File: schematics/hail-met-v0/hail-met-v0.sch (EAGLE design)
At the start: 102 parts, among them IC1 MCP73871, J1 AVR_SPI_PRG_6PTH, U1 ATMEGA328P, Y1 16MHZ

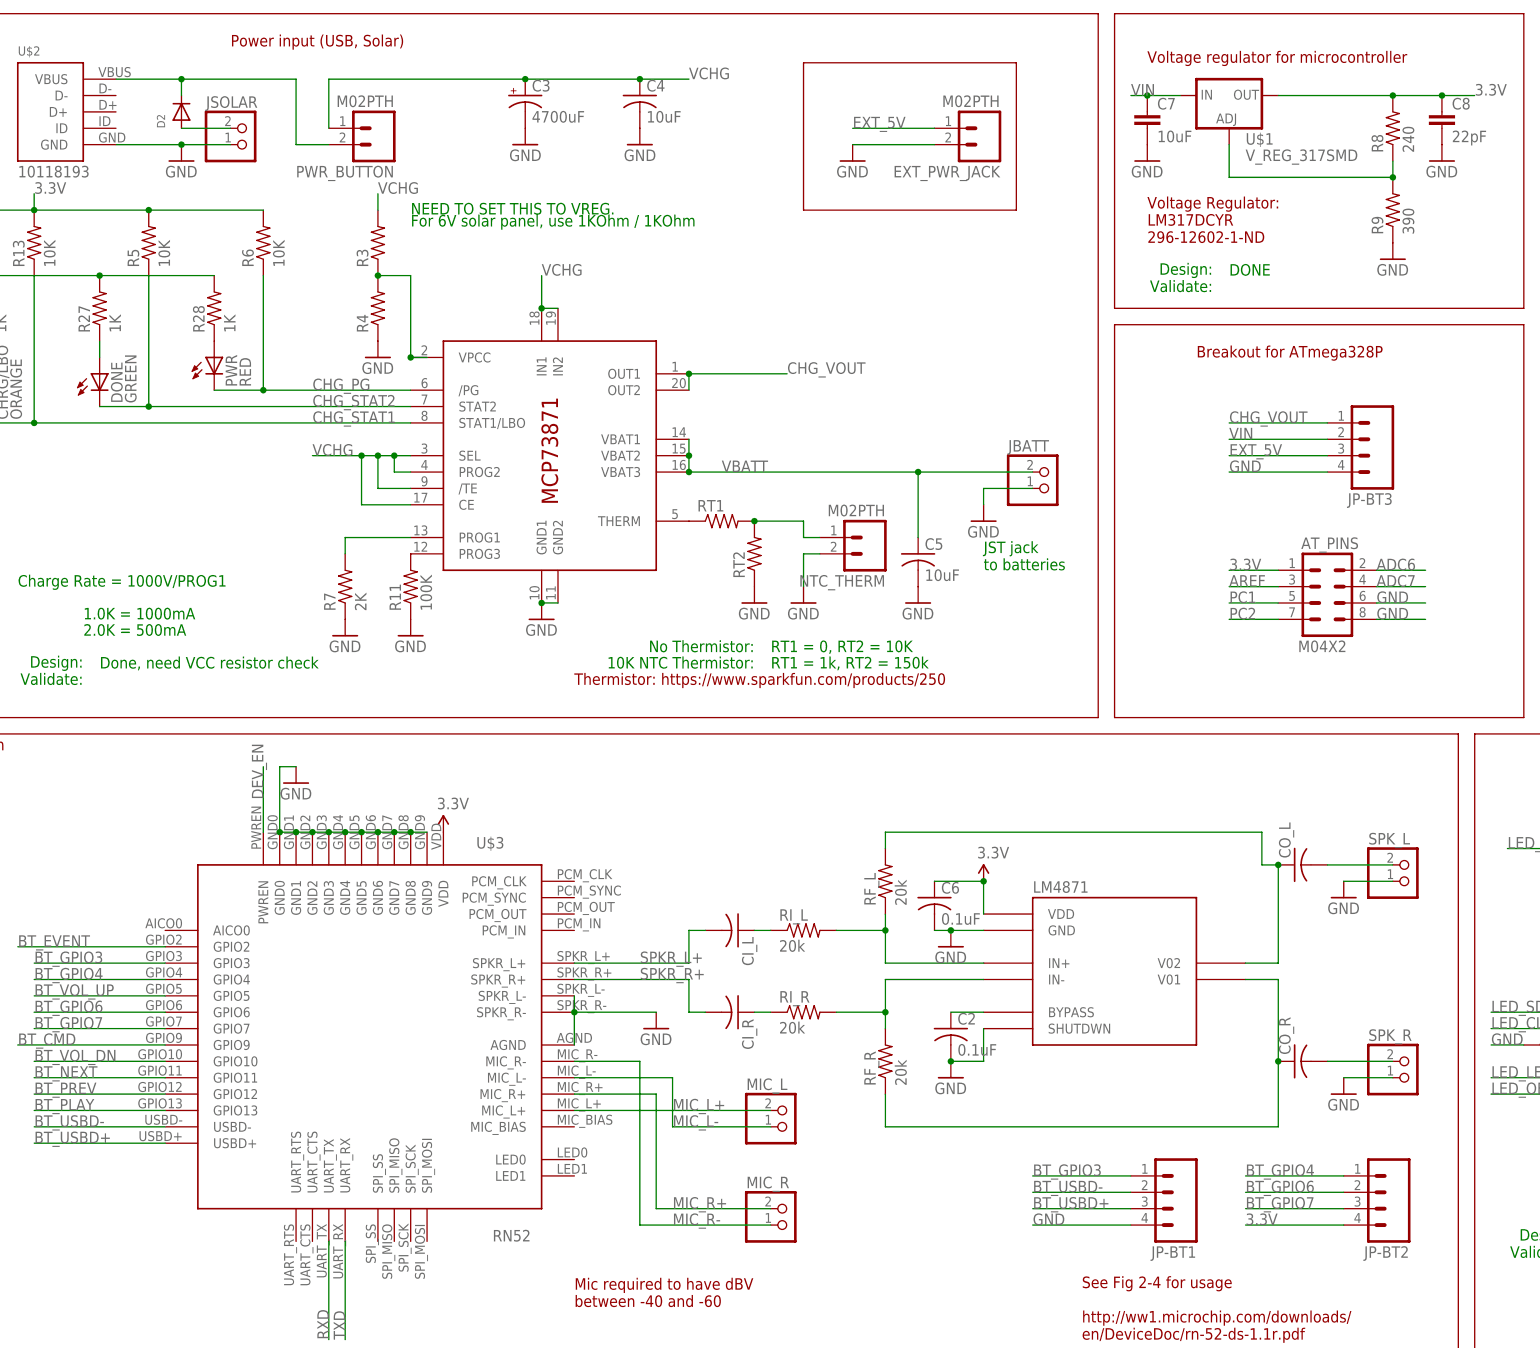
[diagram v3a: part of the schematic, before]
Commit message: added to layout
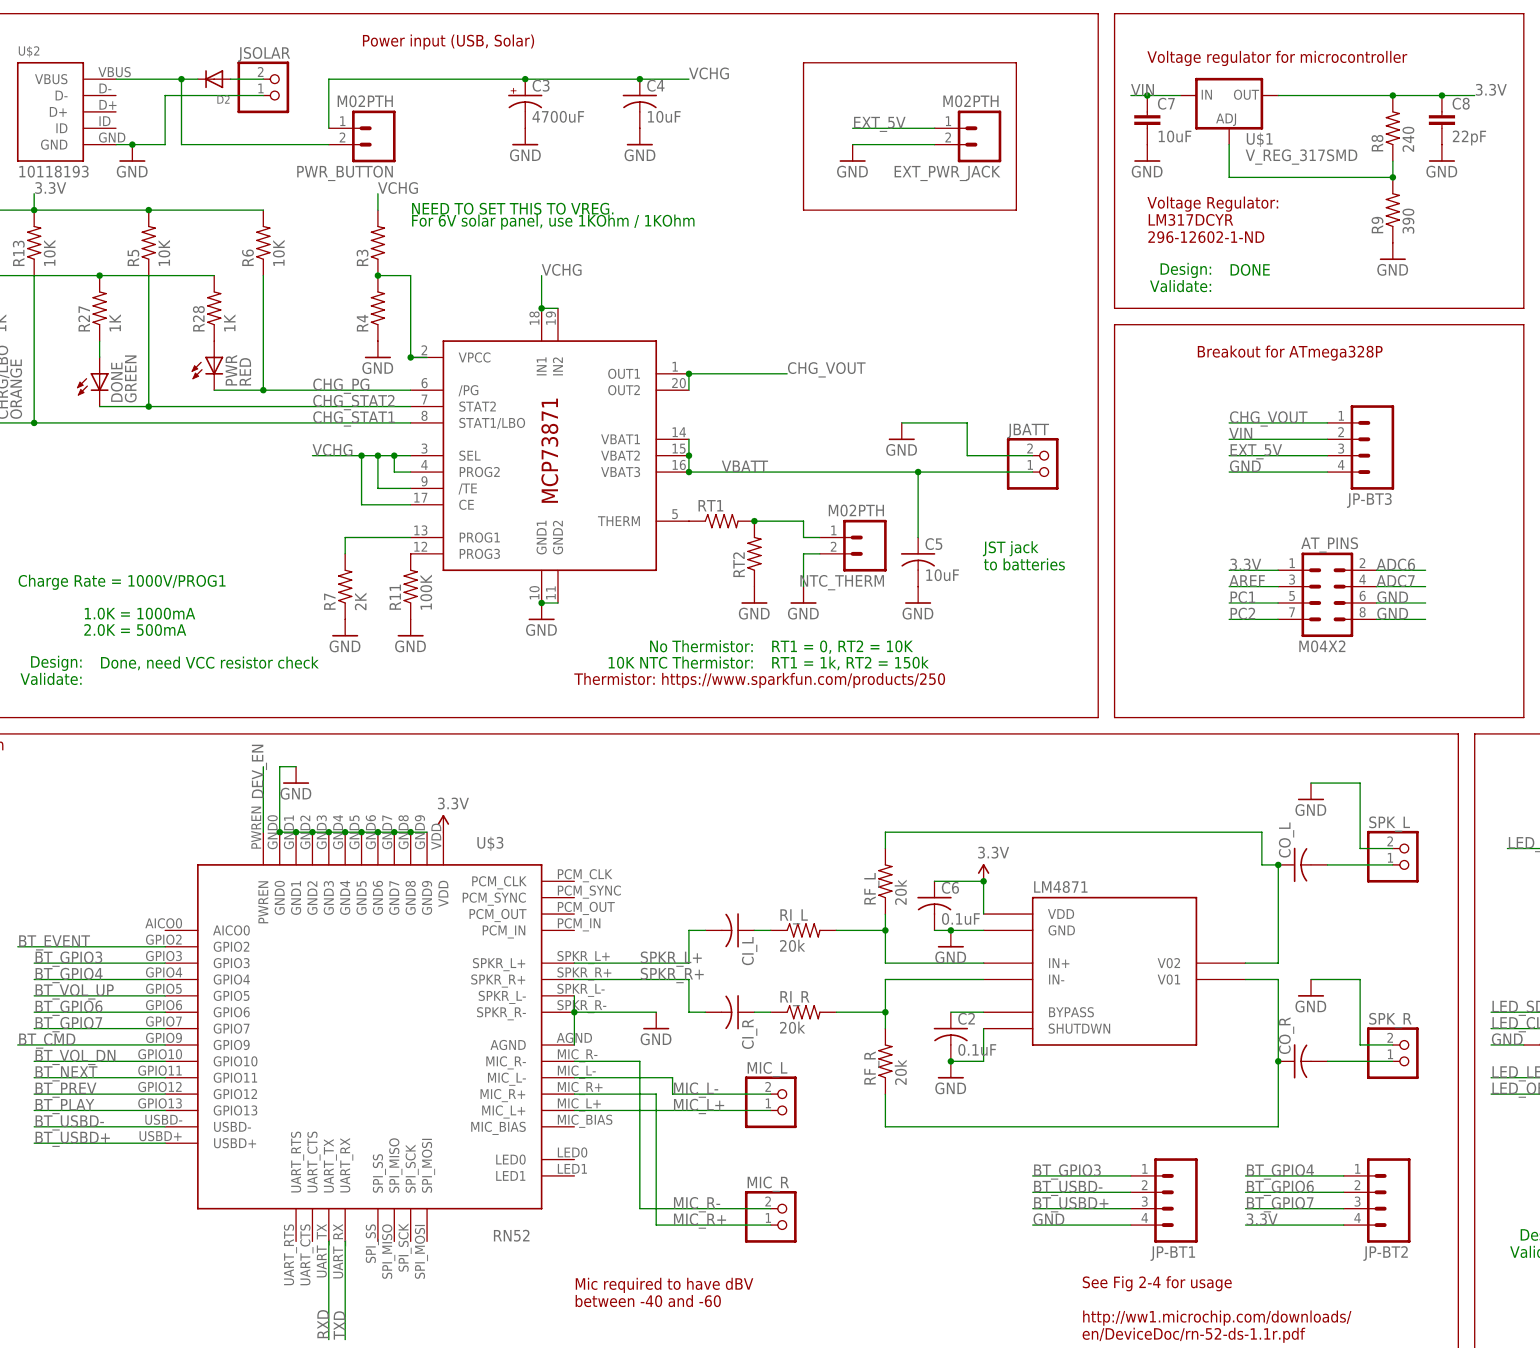
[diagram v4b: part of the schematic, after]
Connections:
- removed net N$27: CO_R.2, SPK_R.1
- new net N$26: CO_R.2, SPK_R.2
- net GND: now also JBATT.1, SPK_L.1, SPK_R.1; no longer JBATT.2, SPK_L.2, SPK_R.2
- net MIC_L+: now also MIC_L.2; no longer MIC_L.1
- net MIC_L-: now also MIC_L.1; no longer MIC_L.2
- net MIC_R+: now also MIC_R.2; no longer MIC_R.1
- net MIC_R-: now also MIC_R.1; no longer MIC_R.2
- net N$14: now also SPK_L.2; no longer SPK_L.1
- net VBATT: now also JBATT.2; no longer JBATT.1
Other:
- moved on the sheet: D2, JBATT, JSOLAR, MIC_L, SPK_L, SPK_R

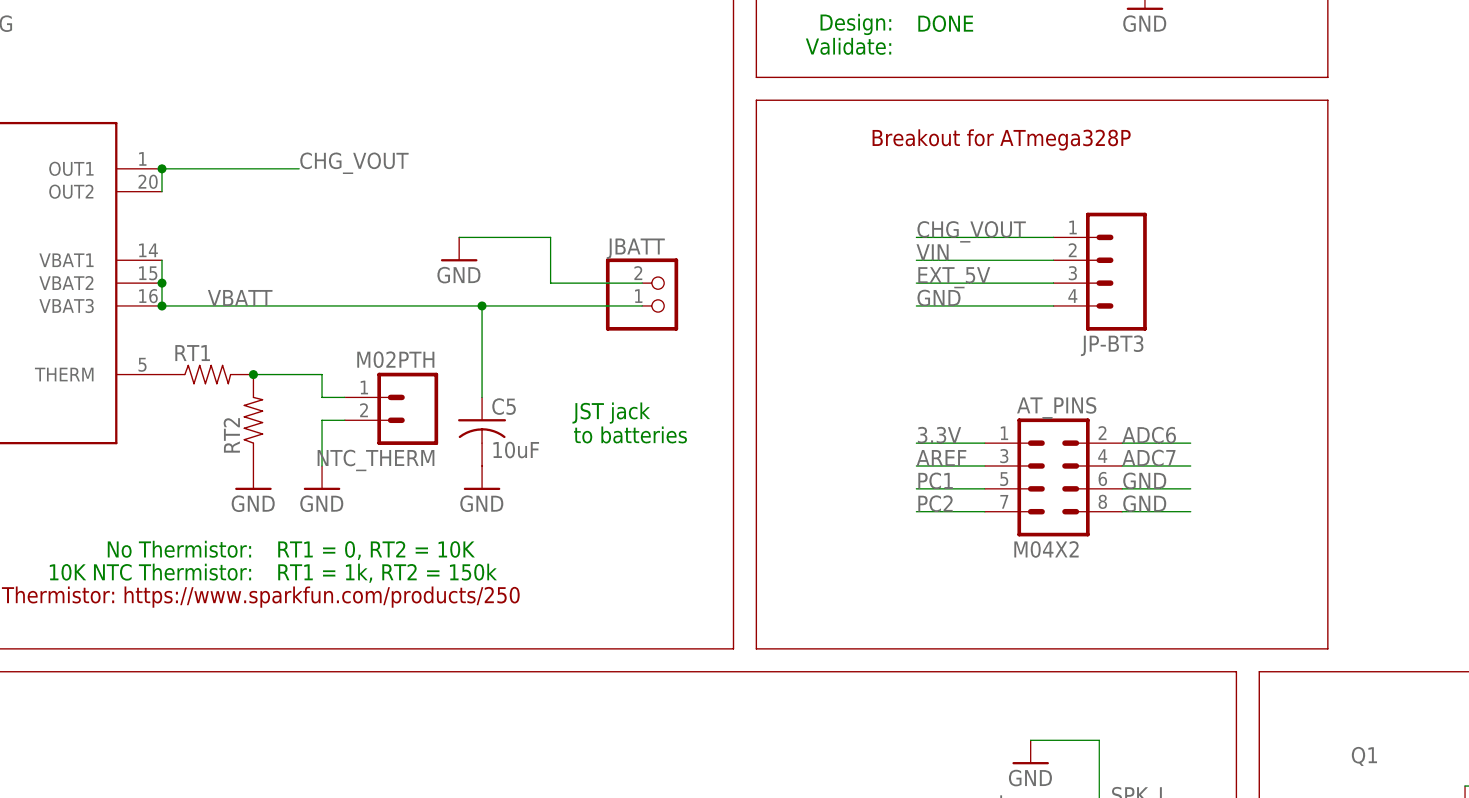
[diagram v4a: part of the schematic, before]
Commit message: added headlight code (NEED TEST) and updated pcb
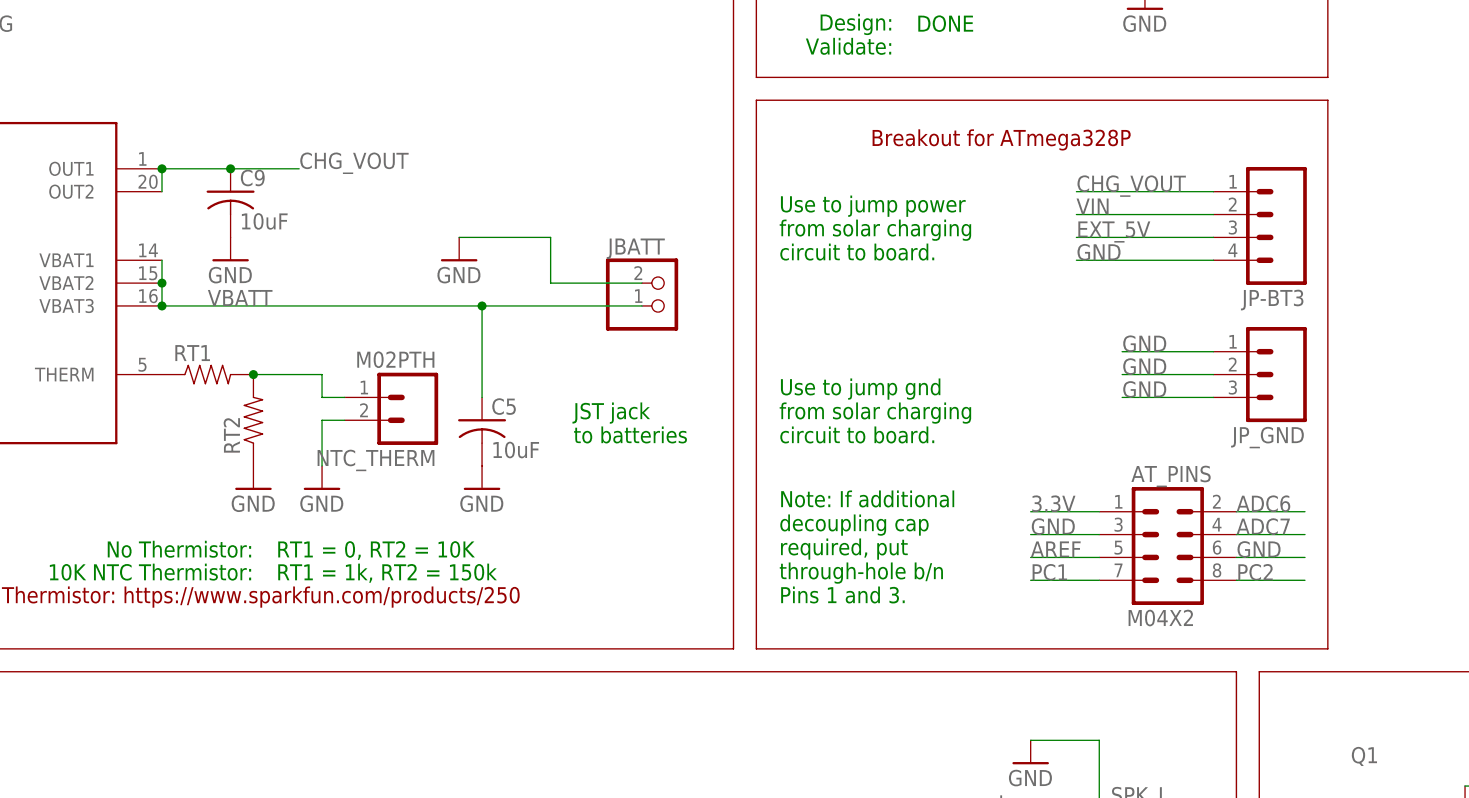
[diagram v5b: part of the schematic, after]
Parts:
- added C9: 10uF, adafruit:C-USC0805K
- added JP_GND: (no value), SparkFun-Connectors:M03LOCK
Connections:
- net AREF: now also AT_PINS.5; no longer AT_PINS.3
- net CHG_VOUT: now also C9.1
- net GND: now also AT_PINS.3, C9.2, JP_GND.1, JP_GND.2, JP_GND.3; no longer AT_PINS.8
- net PC1: now also AT_PINS.7; no longer AT_PINS.5
- net PC2: now also AT_PINS.8; no longer AT_PINS.7
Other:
- note added: "Note: If additional decoupling cap required, put through-hole b/n Pins 1 and 3."
- note added: "Use to jump gnd from solar charging circuit to board."
- note added: "Use to jump power from solar charging circuit to board."
- moved on the sheet: AT_PINS, JP-BT3
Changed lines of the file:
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@@
 <part name="R27" library="SparkFun-Passives" deviceset="RESISTOR" device="0805-RES" value="1K"/>
 <part name="R28" library="SparkFun-Passives" deviceset="RESISTOR" device="0805-RES" value="1K"/>
+<part name="JP_GND" library="SparkFun-Connectors" deviceset="M03" device="LOCK"/>
+<part name="C9" library="adafruit" deviceset="C-US" device="C0805K" value="10uF"/>
+<part name="GND41" library="SparkFun" deviceset="GND" device=""/>
 </parts>
 <sheets>
@@
 <text x="10.16" y="50.8" size="1.778" layer="94">Breakout for ATmega328P</text>
 <text x="162.56" y="76.2" size="1.778" layer="94">x</text>
+<text x="0" y="0" size="1.778" layer="91">Note: If additional
+decoupling cap
+required, put
+through-hole b/n
+Pins 1 and 3.</text>
+<text x="0" y="17.78" size="1.778" layer="91">Use to jump gnd
+from solar charging
+circuit to board.</text>
+<text x="0" y="38.1" size="1.778" layer="91">Use to jump power
+from solar charging
+circuit to board.</text>
 </plain>
 <instances>
@@
 <instance part="R24" gate="G$1" x="193.04" y="-83.82" rot="R180"/>
 <instance part="GND39" gate="1" x="182.88" y="-86.36"/>
-<instance part="JP-BT3" gate="G$1" x="35.56" y="38.1" rot="R180"/>
-<instance part="AT_PINS" gate="G$1" x="30.48" y="12.7"/>
+<instance part="JP-BT3" gate="G$1" x="53.34" y="43.18" rot="R180"/>
+<instance part="AT_PINS" gate="G$1" x="43.18" y="5.08"/>
 <instance part="NOT-GATE" gate="A" x="264.16" y="-27.94"/>
 <instance part="D2" gate="G$1" x="-142.24" y="93.98" rot="R180"/>
@@
 <instance part="R27" gate="G$1" x="-160.02" y="58.42" rot="R90"/>
 <instance part="R28" gate="G$1" x="-142.24" y="58.42" rot="R90"/>
+<instance part="JP_GND" gate="G$1" x="55.88" y="25.4" rot="R180"/>
+<instance part="C9" gate="G$1" x="-60.96" y="45.72"/>
+<instance part="GND41" gate="1" x="-60.96" y="38.1"/>
 </instances>
 <busses>
@@
 </segment>
 <segment>
-<wire x1="15.24" y1="33.02" x2="30.48" y2="33.02" width="0.1524" layer="91"/>
-<label x="15.24" y="33.02" size="1.778" layer="95"/>
+<wire x1="33.02" y1="38.1" x2="48.26" y2="38.1" width="0.1524" layer="91"/>
+<label x="33.02" y="38.1" size="1.778" layer="95"/>
 <pinref part="JP-BT3" gate="G$1" pin="4"/>
 </segment>
 <segment>
-<pinref part="AT_PINS" gate="G$1" pin="8"/>
-<wire x1="45.72" y1="10.16" x2="38.1" y2="10.16" width="0.1524" layer="91"/>
-<label x="38.1" y="10.16" size="1.778" layer="95"/>
-</segment>
-<segment>
 <pinref part="AT_PINS" gate="G$1" pin="6"/>
-<wire x1="38.1" y1="12.7" x2="45.72" y2="12.7" width="0.1524" layer="91"/>
-<label x="38.1" y="12.7" size="1.778" layer="95"/>
+<wire x1="50.8" y1="5.08" x2="58.42" y2="5.08" width="0.1524" layer="91"/>
+<label x="50.8" y="5.08" size="1.778" layer="95"/>
 </segment>
 <segment>
@@
 <wire x1="35.56" y1="-55.88" x2="40.64" y2="-55.88" width="0.1524" layer="91"/>
 </segment>
+<segment>
+<pinref part="JP_GND" gate="G$1" pin="1"/>
+<wire x1="48.26" y1="27.94" x2="38.1" y2="27.94" width="0.1524" layer="91"/>
+<label x="38.1" y="27.94" size="1.778" layer="95"/>
+</segment>
+<segment>
+<pinref part="JP_GND" gate="G$1" pin="2"/>
+<wire x1="38.1" y1="25.4" x2="48.26" y2="25.4" width="0.1524" layer="91"/>
+<label x="38.1" y="25.4" size="1.778" layer="95"/>
+</segment>
+<segment>
+<pinref part="JP_GND" gate="G$1" pin="3"/>
+<wire x1="48.26" y1="22.86" x2="38.1" y2="22.86" width="0.1524" layer="91"/>
+<label x="38.1" y="22.86" size="1.778" layer="95"/>
+</segment>
+<segment>
+<pinref part="AT_PINS" gate="G$1" pin="3"/>
+<wire x1="27.94" y1="7.62" x2="35.56" y2="7.62" width="0.1524" layer="91"/>
+<label x="27.94" y="7.62" size="1.778" layer="95"/>
+</segment>
+<segment>
+<pinref part="C9" gate="G$1" pin="2"/>
+<pinref part="GND41" gate="1" pin="GND"/>
+</segment>
 </net>
 <net name="VIN" class="0">
 <segment>
-<wire x1="30.48" y1="38.1" x2="15.24" y2="38.1" width="0.1524" layer="91"/>
-<label x="15.24" y="38.1" size="1.778" layer="95"/>
+<wire x1="48.26" y1="43.18" x2="33.02" y2="43.18" width="0.1524" layer="91"/>
+<label x="33.02" y="43.18" size="1.778" layer="95"/>
 <pinref part="JP-BT3" gate="G$1" pin="2"/>
 </segment>
@@
 <segment>
 <pinref part="AT_PINS" gate="G$1" pin="1"/>
-<wire x1="22.86" y1="17.78" x2="15.24" y2="17.78" width="0.1524" layer="91"/>
-<label x="15.24" y="17.78" size="1.778" layer="95"/>
+<wire x1="35.56" y1="10.16" x2="27.94" y2="10.16" width="0.1524" layer="91"/>
+<label x="27.94" y="10.16" size="1.778" layer="95"/>
 </segment>
 </net>
@@
 </segment>
 <segment>
-<pinref part="AT_PINS" gate="G$1" pin="3"/>
-<wire x1="15.24" y1="15.24" x2="22.86" y2="15.24" width="0.1524" layer="91"/>
-<label x="15.24" y="15.24" size="1.778" layer="95"/>
+<pinref part="AT_PINS" gate="G$1" pin="5"/>
+<wire x1="27.94" y1="5.08" x2="35.56" y2="5.08" width="0.1524" layer="91"/>
+<label x="27.94" y="5.08" size="1.778" layer="95"/>
 </segment>
 </net>
@@
 <wire x1="-68.58" y1="45.72" x2="-68.58" y2="48.26" width="0.1524" layer="91"/>
 <label x="-53.34" y="48.26" size="1.778" layer="95"/>
-<wire x1="-68.58" y1="48.26" x2="-53.34" y2="48.26" width="0.1524" layer="91"/>
+<wire x1="-68.58" y1="48.26" x2="-60.96" y2="48.26" width="0.1524" layer="91"/>
 <junction x="-68.58" y="48.26"/>
-</segment>
-<segment>
-<wire x1="15.24" y1="40.64" x2="30.48" y2="40.64" width="0.1524" layer="91"/>
-<label x="15.24" y="40.64" size="1.778" layer="95"/>
+<pinref part="C9" gate="G$1" pin="1"/>
+<wire x1="-60.96" y1="48.26" x2="-53.34" y2="48.26" width="0.1524" layer="91"/>
+<junction x="-60.96" y="48.26"/>
+</segment>
+<segment>
+<wire x1="33.02" y1="45.72" x2="48.26" y2="45.72" width="0.1524" layer="91"/>
+<label x="33.02" y="45.72" size="1.778" layer="95"/>
 <pinref part="JP-BT3" gate="G$1" pin="1"/>
 </segment>
@@
 </segment>
 <segment>
-<wire x1="15.24" y1="35.56" x2="30.48" y2="35.56" width="0.1524" layer="91"/>
-<label x="15.24" y="35.56" size="1.778" layer="95"/>
+<wire x1="33.02" y1="40.64" x2="48.26" y2="40.64" width="0.1524" layer="91"/>
+<label x="33.02" y="40.64" size="1.778" layer="95"/>
 <pinref part="JP-BT3" gate="G$1" pin="3"/>
 </segment>
@@
 </segment>
 <segment>
-<pinref part="AT_PINS" gate="G$1" pin="5"/>
-<wire x1="15.24" y1="12.7" x2="22.86" y2="12.7" width="0.1524" layer="91"/>
-<label x="15.24" y="12.7" size="1.778" layer="95"/>
+<pinref part="AT_PINS" gate="G$1" pin="7"/>
+<wire x1="27.94" y1="2.54" x2="35.56" y2="2.54" width="0.1524" layer="91"/>
+<label x="27.94" y="2.54" size="1.778" layer="95"/>
 </segment>
 </net>
@@
 </segment>
 <segment>
-<pinref part="AT_PINS" gate="G$1" pin="7"/>
-<wire x1="15.24" y1="10.16" x2="22.86" y2="10.16" width="0.1524" layer="91"/>
-<label x="15.24" y="10.16" size="1.778" layer="95"/>
+<pinref part="AT_PINS" gate="G$1" pin="8"/>
+<wire x1="58.42" y1="2.54" x2="50.8" y2="2.54" width="0.1524" layer="91"/>
+<label x="50.8" y="2.54" size="1.778" layer="95"/>
 </segment>
 </net>
@@
 <segment>
 <pinref part="AT_PINS" gate="G$1" pin="4"/>
-<wire x1="45.72" y1="15.24" x2="38.1" y2="15.24" width="0.1524" layer="91"/>
-<label x="38.1" y="15.24" size="1.778" layer="95"/>
+<wire x1="58.42" y1="7.62" x2="50.8" y2="7.62" width="0.1524" layer="91"/>
+<label x="50.8" y="7.62" size="1.778" layer="95"/>
 </segment>
 <segment>
@@
 <segment>
 <pinref part="AT_PINS" gate="G$1" pin="2"/>
-<wire x1="38.1" y1="17.78" x2="45.72" y2="17.78" width="0.1524" layer="91"/>
-<label x="38.1" y="17.78" size="1.778" layer="95"/>
-</segment>
-<segment>
+<wire x1="50.8" y1="10.16" x2="58.42" y2="10.16" width="0.1524" layer="91"/>
+<label x="50.8" y="10.16" size="1.778" layer="95"/>
+</segment>
+<segment>
